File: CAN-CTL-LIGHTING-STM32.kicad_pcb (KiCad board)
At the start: 2 copper layers, 79 x 55 mm, 48 parts, among them J1 H GND L, J2 TERM, J3 USART1, J4 LEDA, J5 PWR IN, J6 LEDB, J7 LEDC, J8 LEDD, U1 STM32G0B1RCTx, U2 MCP2562-E-SN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

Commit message: drc passed
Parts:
- U1: value STM32G0B1RCTx -> STM32G0B1
- renumbered RRFBB1 to RFBB1
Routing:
- net GND: vias 95 -> 198

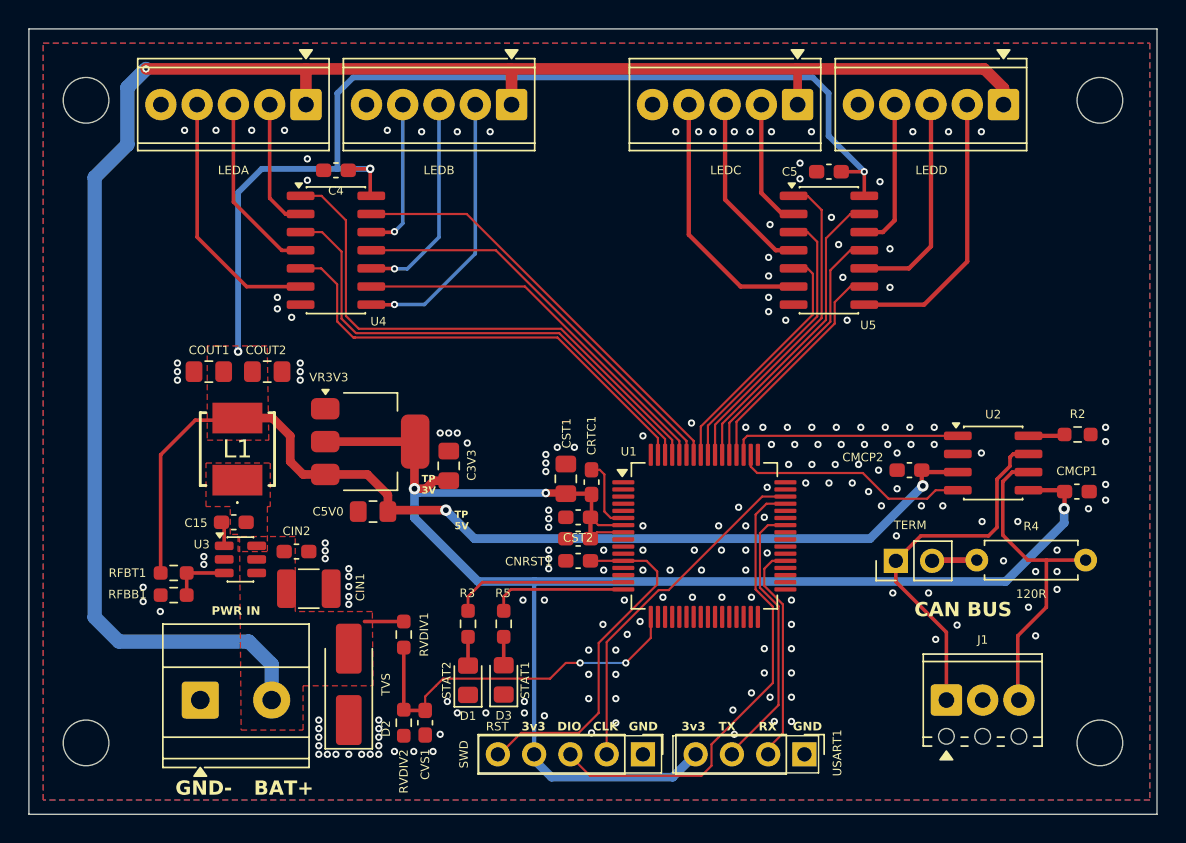
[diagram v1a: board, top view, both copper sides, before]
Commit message: silkscreen updates, swapped ground and H on can connector
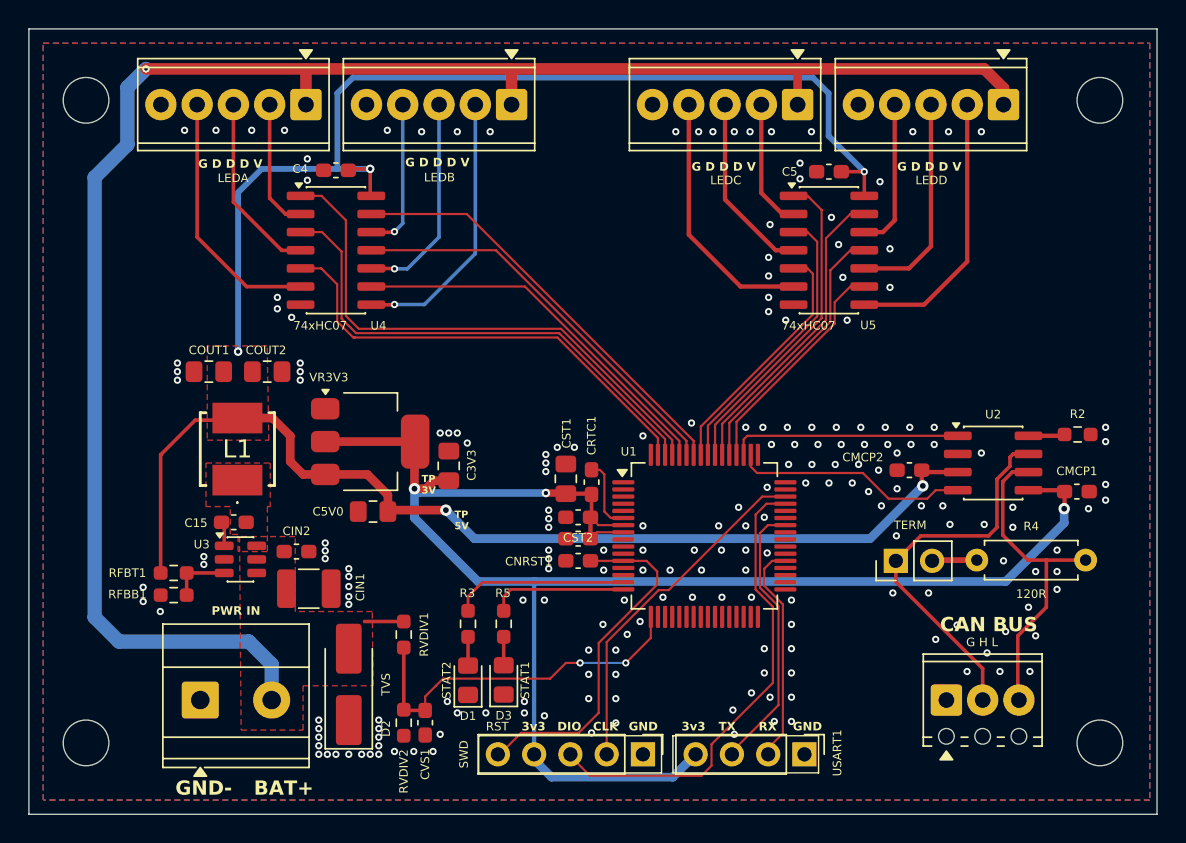
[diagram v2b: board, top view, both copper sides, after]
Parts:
- J1: value H GND L -> G H L
- U4, U5: value 74LS07 -> 74xHC07
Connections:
- J1 pad 1: /CANH -> GND
- J1 pad 2: GND -> /CANH
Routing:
- net /CANH: track 25.9 -> 27.0 mm
- net GND: vias 198 -> 205
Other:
- board text added: "G D D D V"
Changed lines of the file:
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@@
 			(at 2.54 -4.22 0)
 			(layer "F.SilkS")
+			(hide yes)
 			(effects
 				(font
@@
 			)
 		)
-		(property "Value" "H GND L"
-			(at 2.54 4.22 0)
-			(layer "F.Fab")
+		(property "Value" "G H L"
+			(at 2.5 -4.05 0)
+			(layer "F.SilkS")
 			(effects
 				(font
@@
 			(remove_unused_layers no)
 			(roundrect_rratio 0.113636)
-			(net 13 "/CANH")
+			(net 1 "GND")
 			(pinfunction "Pin_1")
 			(pintype "passive")
@@
 			(layers "*.Cu" "*.Mask")
 			(remove_unused_layers no)
-			(net 1 "GND")
+			(net 13 "/CANH")
 			(pinfunction "Pin_2")
 			(pintype "passive")
@@
 			)
 		)
-		(property "Value" "74LS07"
-			(at 0 5.28 0)
-			(layer "F.Fab")
-			(hide yes)
+		(property "Value" "74xHC07"
+			(at -1.425 5.28 0)
+			(layer "F.SilkS")
 			(effects
 				(font
@@
 		(tags "SOIC SO")
 		(property "Reference" "U4"
-			(at 2.975 4.99 0)
+			(at 2.975 5.28 0)
 			(layer "F.SilkS")
 			(effects
@@
 			)
 		)
-		(property "Value" "74LS07"
-			(at 0 5.28 0)
-			(layer "F.Fab")
-			(hide yes)
+		(property "Value" "74xHC07"
+			(at -1.1 5.28 0)
+			(layer "F.SilkS")
 			(effects
 				(font
@@
 		)
 		(property "Value" "LEDD"
-			(at 5.05 -4.6 0)
+			(at 5.05 -5.3 0)
 			(layer "F.SilkS")
 			(effects
@@
 		)
 		(property "Value" "LEDB"
-			(at 5.08 -4.6 0)
+			(at 5.05 -5.1 0)
 			(layer "F.SilkS")
 			(effects
@@
 		)
 		(property "Value" "LEDA"
-			(at 5.08 -4.6 0)
+			(at 5.1 -5.15 0)
 			(layer "F.SilkS")
 			(effects
@@
 		)
 		(property "Value" "LEDC"
-			(at 5.03 -4.6 0)
+			(at 5.03 -5.3 0)
 			(layer "F.SilkS")
 			(effects
@@
 		(tags "capacitor handsolder")
 		(property "Reference" "C4"
-			(at 0 -1.43 0)
+			(at 2.5 0.1 0)
 			(layer "F.SilkS")
 			(effects
@@
 		)
 	)
+	(gr_text "G D D D V"
+		(at 143.4 85 0)
+		(layer "F.SilkS")
+		(effects
+			(font
+				(size 0.6 0.6)
+				(thickness 0.1)
+				(bold yes)
+			)
+			(justify left bottom)
+		)
+	)
 	(gr_text "TX"
 		(at 145.3 124.2 0)
@@
 		)
 	)
+	(gr_text "G D D D V"
+		(at 108.85 84.8 0)
+		(layer "F.SilkS")
+		(effects
+			(font
+				(size 0.6 0.6)
+				(thickness 0.1)
+				(bold yes)
+			)
+			(justify left bottom)
+		)
+	)
 	(gr_text "3v3"
 		(at 131.5 124.2 0)
@@
 	)
 	(gr_text "CAN BUS"
-		(at 159 116.25 0)
+		(at 160.8 117.3 0)
 		(layer "F.SilkS")
 		(effects
@@
 		)
 	)
+	(gr_text "G D D D V"
+		(at 123.35 84.7 0)
+		(layer "F.SilkS")
+		(effects
+			(font
+				(size 0.6 0.6)
+				(thickness 0.1)
+				(bold yes)
+			)
+			(justify left bottom)
+		)
+	)
+	(gr_text "G D D D V"
+		(at 157.8 85 0)
+		(layer "F.SilkS")
+		(effects
+			(font
+				(size 0.6 0.6)
+				(thickness 0.1)
+				(bold yes)
+			)
+			(justify left bottom)
+		)
+	)
 	(gr_text "DIO"
 		(at 134 124.2 0)
@@
 	)
 	(via
-		(at 166.25 109.5)
+		(at 165.9 109.9)
 		(size 0.508)
 		(drill 0.254)
@@
 	)
 	(via
+		(at 165.4 117.2)
+		(size 0.508)
+		(drill 0.254)
+		(layers "F.Cu" "B.Cu")
+		(free yes)
+		(net 1)
+	)
+	(via
 		(at 142.3 82.2)
 		(size 0.508)
@@
 	)
 	(via
+		(at 164.1 118.7)
+		(size 0.508)
+		(drill 0.254)
+		(layers "F.Cu" "B.Cu")
+		(free yes)
+		(net 1)
+	)
+	(via
 		(at 146.4 82.2)
 		(size 0.508)
@@
 	)
 	(via
+		(at 161.5 109.7)
+		(size 0.508)
+		(drill 0.254)
+		(layers "F.Cu" "B.Cu")
+		(free yes)
+		(net 1)
+	)
+	(via
 		(at 127 82.2)
 		(size 0.508)
@@
 	)
 	(via
+		(at 165.9 108.5)
+		(size 0.508)
+		(drill 0.254)
+		(layers "F.Cu" "B.Cu")
+		(free yes)
+		(net 1)
+	)
+	(via
 		(at 140 103.5)
 		(size 0.508)
@@
 	)
 	(via
+		(at 162.7 120)
+		(size 0.508)
+		(drill 0.254)
+		(layers "F.Cu" "B.Cu")
+		(free yes)
+		(net 1)
+	)
+	(via
 		(at 157.75 110.5)
 		(size 0.508)
@@
 	)
 	(via
+		(at 167.1 120)
+		(size 0.508)
+		(drill 0.254)
+		(layers "F.Cu" "B.Cu")
+		(free yes)
+		(net 1)
+	)
+	(via
 		(at 148.5 118.4)
 		(size 0.508)
@@
 	)
 	(via
+		(at 165 120)
+		(size 0.508)
+		(drill 0.254)
+		(layers "F.Cu" "B.Cu")
+		(free yes)
+		(net 1)
+	)
+	(via
 		(at 145.533333 114.8)
 		(size 0.508)
@@
 	)
 	(via
-		(at 163.75 109.5)
+		(at 163.9 109.7)
 		(size 0.508)
 		(drill 0.254)
@@
 	)
 	(segment
-		(start 164.7926 106.53125)
-		(end 165.7 105.62385)
+		(start 163.79 119.79)
+		(end 163.79 122)
 		(width 0.254)
 		(layer "F.Cu")
@@
 	)
 	(segment
-		(start 165.935 104.765)
-		(end 167 104.765)
+		(start 164.7926 106.53125)
+		(end 165.7 105.62385)
 		(width 0.254)
 		(layer "F.Cu")
@@
 	)
 	(segment
-		(start 157.71 113.71)
-		(end 157.71 112.25)
+		(start 165.935 104.765)
+		(end 167 104.765)
 		(width 0.254)
 		(layer "F.Cu")
@@
 	)
 	(segment
-		(start 161.25 122)
-		(end 161.25 117.25)
-		(width 0.254)
-		(layer "F.Cu")
-		(net 13)
-	)
-	(segment
 		(start 165.7 105)
 		(end 165.935 104.765)
@@
 	)
 	(segment
-		(start 161.25 117.25)
-		(end 157.71 113.71)
+		(start 157.71 113.71)
+		(end 163.79 119.79)
 		(width 0.254)
 		(layer "F.Cu")
@@
 		(width 0.254)
 		(layer "F.Cu")
+		(net 13)
+	)
+	(segment
+		(start 157.71 112.25)
+		(end 157.71 113.71)
+		(width 0.254)
+		(layer "F.Cu")

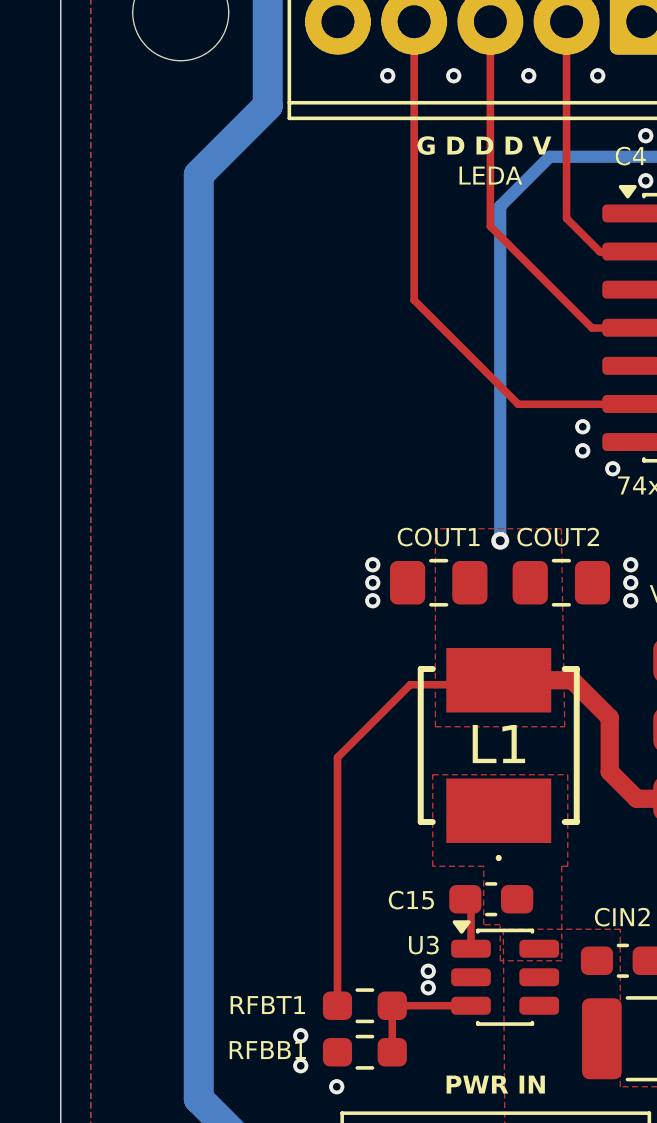
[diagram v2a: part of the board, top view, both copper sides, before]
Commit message: added copyright text
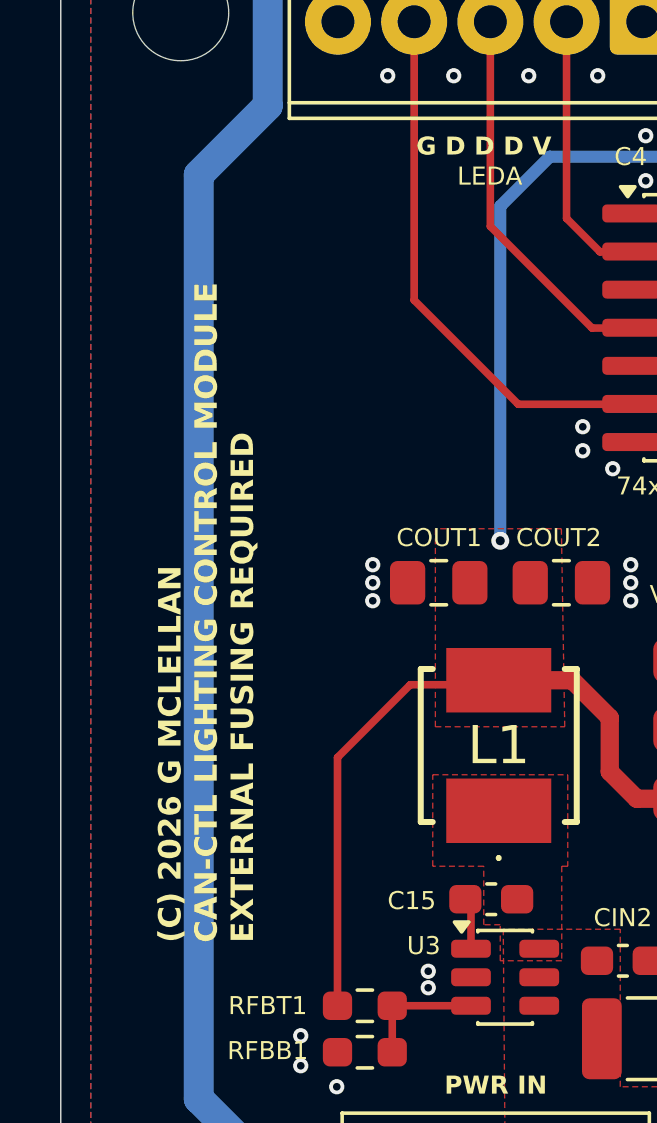
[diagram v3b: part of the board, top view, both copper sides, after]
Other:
- board text added: "(C) 2026 G MCLELLAN CAN-CTL LIGHTING CONTROL MODULE EXTERNAL FUSING REQUIRED"
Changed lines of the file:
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@@
 		(layer "Edge.Cuts")
+	)
+	(gr_text "(C) 2026 G MCLELLAN\nCAN-CTL LIGHTING CONTROL MODULE\nEXTERNAL FUSING REQUIRED"
+		(at 103.5 111 90)
+		(layer "F.SilkS")
+		(effects
+			(font
+				(size 0.75 0.75)
+				(thickness 0.15)
+				(bold yes)
+			)
+			(justify left bottom)
+		)
 	)
 	(gr_text "GND"

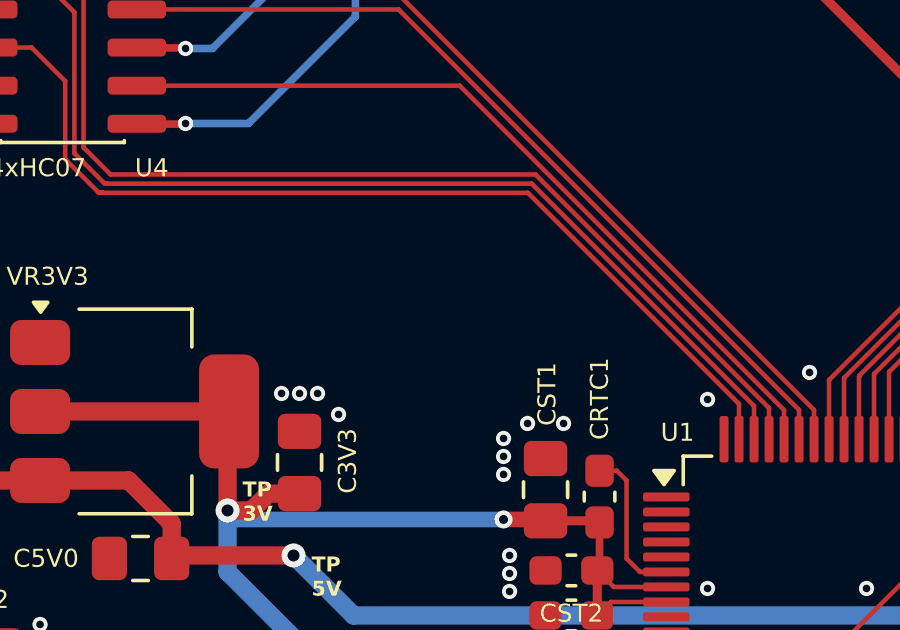
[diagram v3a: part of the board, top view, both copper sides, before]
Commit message: added crystal osc
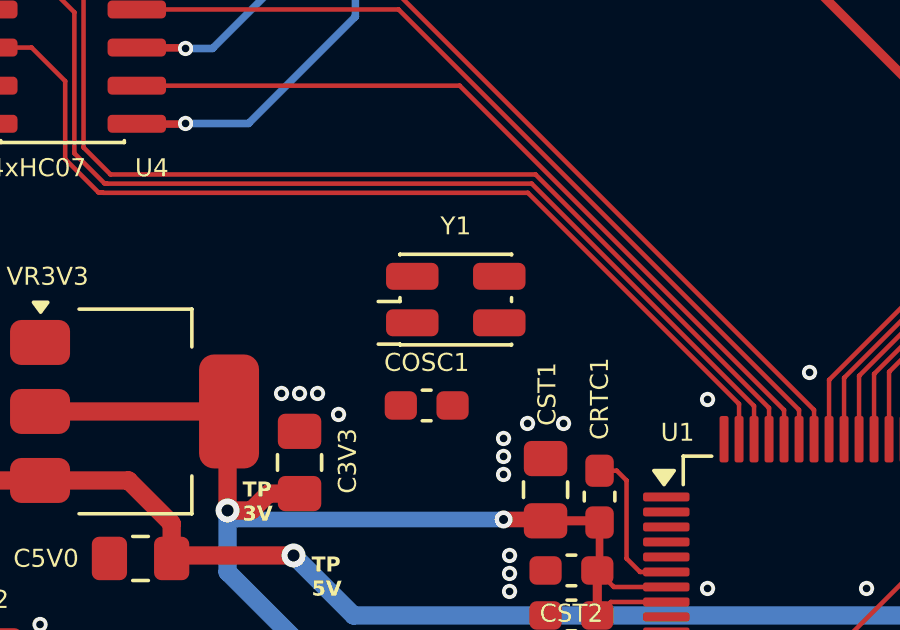
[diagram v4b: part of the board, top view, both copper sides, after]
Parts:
- added COSC1: 100n, Capacitor_SMD:C_0603_1608Metric_Pad1.08x0.95mm_HandSolder, F.Cu at (130.6, 103.7)
- added Y1: 8MHz, Oscillator:Oscillator_SMD_EuroQuartz_XO32-4Pin_3.2x2.5mm_RotB_HandSoldering, F.Cu at (131.6, 100.2)
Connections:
- U1 pad 10: unconnected-(U1-PF0-Pad10) -> /OSC

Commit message: drc passed
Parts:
- moved Y1 12.0 mm to (130.4, 112.1)
- moved COSC1 9.17 mm to (126.9, 112.1), turned to -90 degrees
- moved CNRST1 1.05 mm to (135.5, 113.3)
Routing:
- net /OSC: track 0.00 -> 7.24 mm
- net +3.3V: track 113.7 -> 118.5 mm, vias 3 -> 4
- net +5V: track 148.3 -> 147.6 mm
- net GND: vias 205 -> 209
